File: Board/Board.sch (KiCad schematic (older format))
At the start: 14 parts

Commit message: Schematic and BOM almost done
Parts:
- removed MK?: Microphone, symbol Device:Microphone
- added C3, C7, C8: 100nF, Capacitor_SMD:C_0603_1608Metric, symbol Device:C
- added C6: 1000uF, symbol Device:C
- added D1: RED, LED_SMD:LED_0805_2012Metric, symbol Device:LED
- added MK1: IM69D120, Sensor_Audio:Infineon_PG-LLGA-5-1, symbol Sensor_Audio:IM69D120
- added Q1, Q2: Q_NMOS_GSD, Package_TO_SOT_SMD:SOT-23, symbol Device:Q_NMOS_GSD
- added R2, R5: 120, Resistor_SMD:R_0603_1608Metric, symbol Device:R
- added R3, R6: 510, Resistor_SMD:R_0603_1608Metric, symbol Device:R
- added R4: 3.48, Resistor_SMD:R_2512_6332Metric, symbol Device:R
- added SW2: SW_DIP_x01, symbol Switch:SW_DIP_x01
- added TP1, TP2, TP3, TP4, TP5, TP6: TestPoint, TestPoint:TestPoint_THTPad_D1.0mm_Drill0.5mm, symbol Connector:TestPoint
- BT1: renamed from BT?; footprint (none) -> Battery:BatteryHolder_Keystone_103_1x20mm
- C1, C4, C5: renamed from C?; footprint (none) -> Capacitor_SMD:C_0603_1608Metric
- C2: renamed from C?; value 22uF -> 33uF; footprint (none) -> Capacitor_SMD:C_0603_1608Metric
- J1: renamed from J?; footprint (none) -> Connector_Card:microSD_HC_Wuerth_693072010801
- L1: renamed from L?; footprint (none) -> Inductor_SMD:L_1206_3216Metric_Pad1.42x1.75mm_HandSolder
- LS1: renamed from LS?; footprint (none) -> Board:SPKR_CMS-151135-078S-67
- R1: renamed from R?; footprint (none) -> Resistor_SMD:R_0603_1608Metric
- gave numbers to parts that had none: 4
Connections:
- net labels added: +5V, CS, MCU_POWER, MICCLK, MICDATA, MISO, MOSI, RESET, SCK, SDPWR, SD_POWER, SPEAKER
- wire segments 18 -> 61
- no-connect marks 0 -> 15
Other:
- note added: "MICROCONTROLLER"
- note added: "MICROPHONE\n"
- note added: "POWER\n"
- note added: "SD CARD"
- note added: "SPEAKER\n"
- note added: "Should be 100\n"
- note added: "Should be 18pF"
- note added: "Should be 22uF"
- note removed: "TODO: Bien découpler\n"
- moved on the sheet: C1, C2, C4, C5, J1, L1, LS1, R1, U1, U2, Y1

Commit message: Schematic done, components almost selected
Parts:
- removed C3: 100nF, Capacitor_SMD:C_0603_1608Metric, symbol Device:C
- removed SW1: SW_Push, symbol Switch:SW_Push
- removed SW2: SW_DIP_x01, symbol Switch:SW_DIP_x01
- removed TP1, TP2, TP3, TP4, TP5, TP6: TestPoint, TestPoint:TestPoint_THTPad_D1.0mm_Drill0.5mm, symbol Connector:TestPoint
- added H1, H2, H3, H4, H5, H6, H7, H8: MountingHole_Pad, symbol Mechanical:MountingHole_Pad
- added R7: 10k, Resistor_SMD:R_0603_1608Metric, symbol Device:R
- added R?: 68, Resistor_SMD:R_0603_1608Metric, symbol Device:R
- added SW1, SW2: SW_SPST, symbol Switch:SW_SPST
- BT1: footprint Battery:BatteryHolder_Keystone_103_1x20mm -> (none)
- C2: value 33uF -> 22uF
- C4, C5: value 22pF -> 18pF
- R3, R6: value 510 -> 1k
- R5: value 120 -> 68
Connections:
- net labels added: SDGND
- net labels removed: SDPWR
- wire segments 61 -> 62
- no-connect marks 15 -> 14
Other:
- note removed: "Should be 100\n"
- note removed: "Should be 18pF"
- note removed: "Should be 22uF"
- moved on the sheet: C6, J1, LS1, Q1, Q2, R3, R4, R6

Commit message: BOM ready
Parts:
- removed BT1: Battery_Cell, symbol Device:Battery_Cell
- removed H1, H2, H3, H4, H5, H6, H7, H8: MountingHole_Pad, symbol Mechanical:MountingHole_Pad
- removed SW1: SW_SPST, symbol Switch:SW_SPST
- added J2: Conn_01x02_Male, ConnectorsEvo:B02B-PASK, symbol Connector:Conn_01x02_Male
- added TP1, TP2, TP3, TP4, TP5, TP6, TP7, TP8: TestPoint, TestPoint:TestPoint_THTPad_D1.0mm_Drill0.5mm, symbol Connector:TestPoint
- C2: footprint Capacitor_SMD:C_0603_1608Metric -> Capacitor_SMD:C_0805_2012Metric
- C6: footprint (none) -> Capacitor_THT:C_Radial_D8.0mm_H11.5mm_P3.50mm
- L1: footprint Inductor_SMD:L_1206_3216Metric_Pad1.42x1.75mm_HandSolder -> Inductor_SMD:L_1008_2520Metric
- SW2: footprint (none) -> Button_Switch_THT:SW_DIP_SPSTx01_Slide_6.7x4.1mm_W7.62mm_P2.54mm_LowProfile
- Y1: footprint (none) -> Crystal:Crystal_HC49-4H_Vertical
- gave numbers to parts that had none: 1
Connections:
- wire segments 62 -> 59

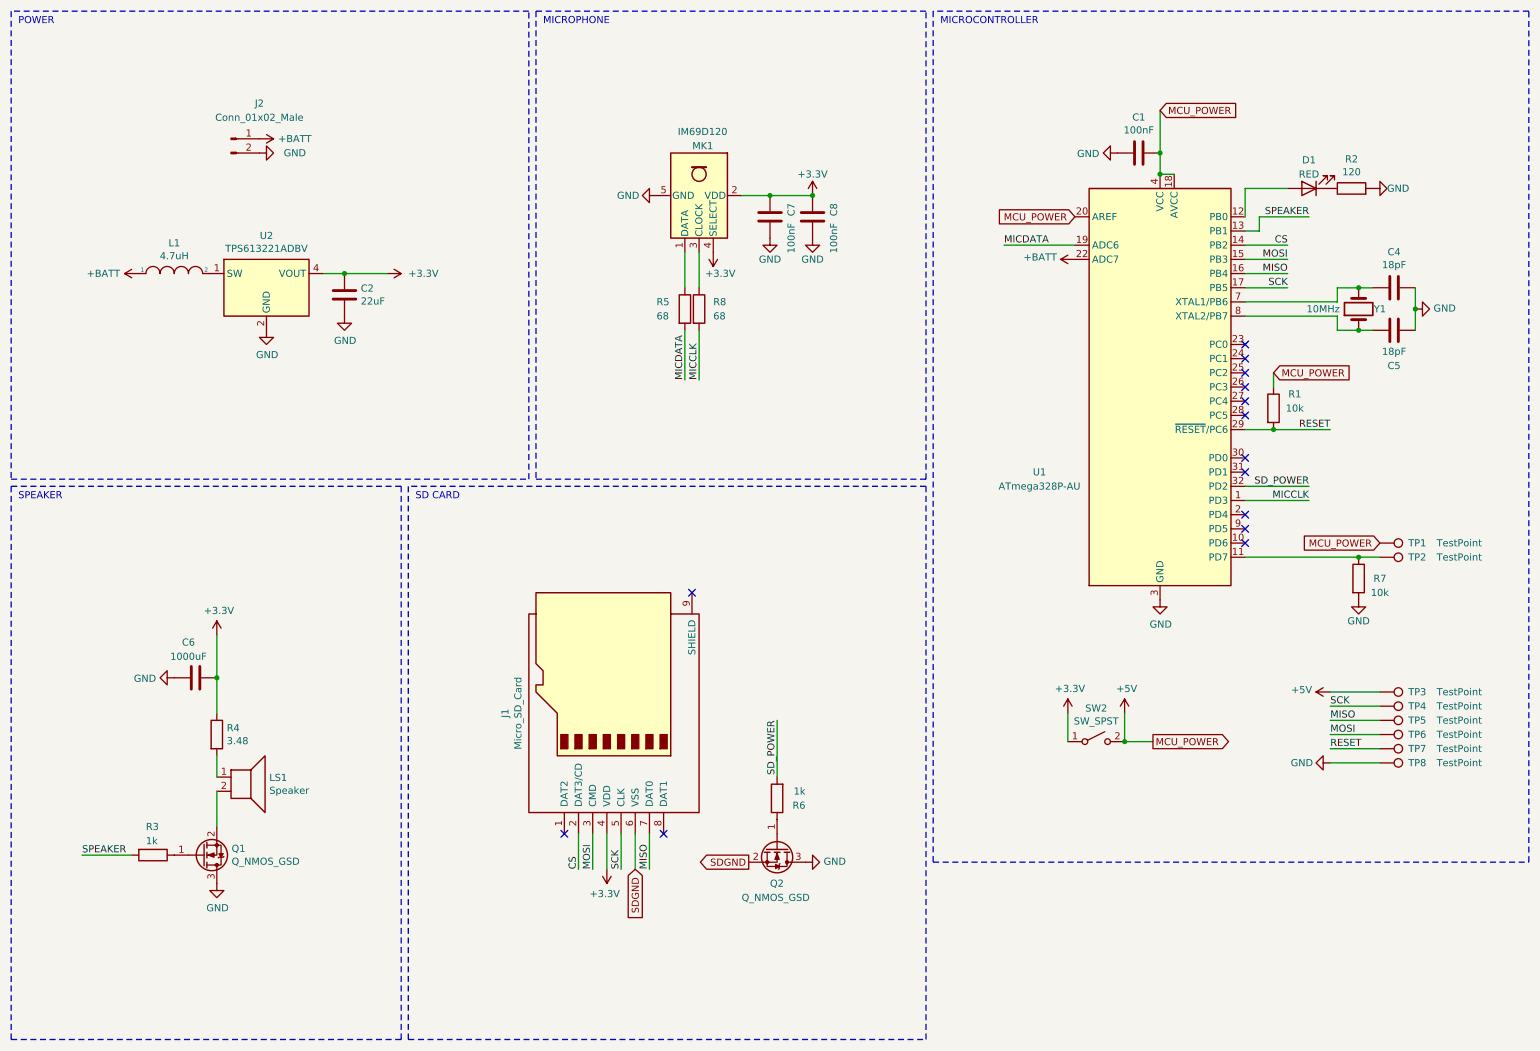
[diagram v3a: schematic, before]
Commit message: Changed components + first layout tests
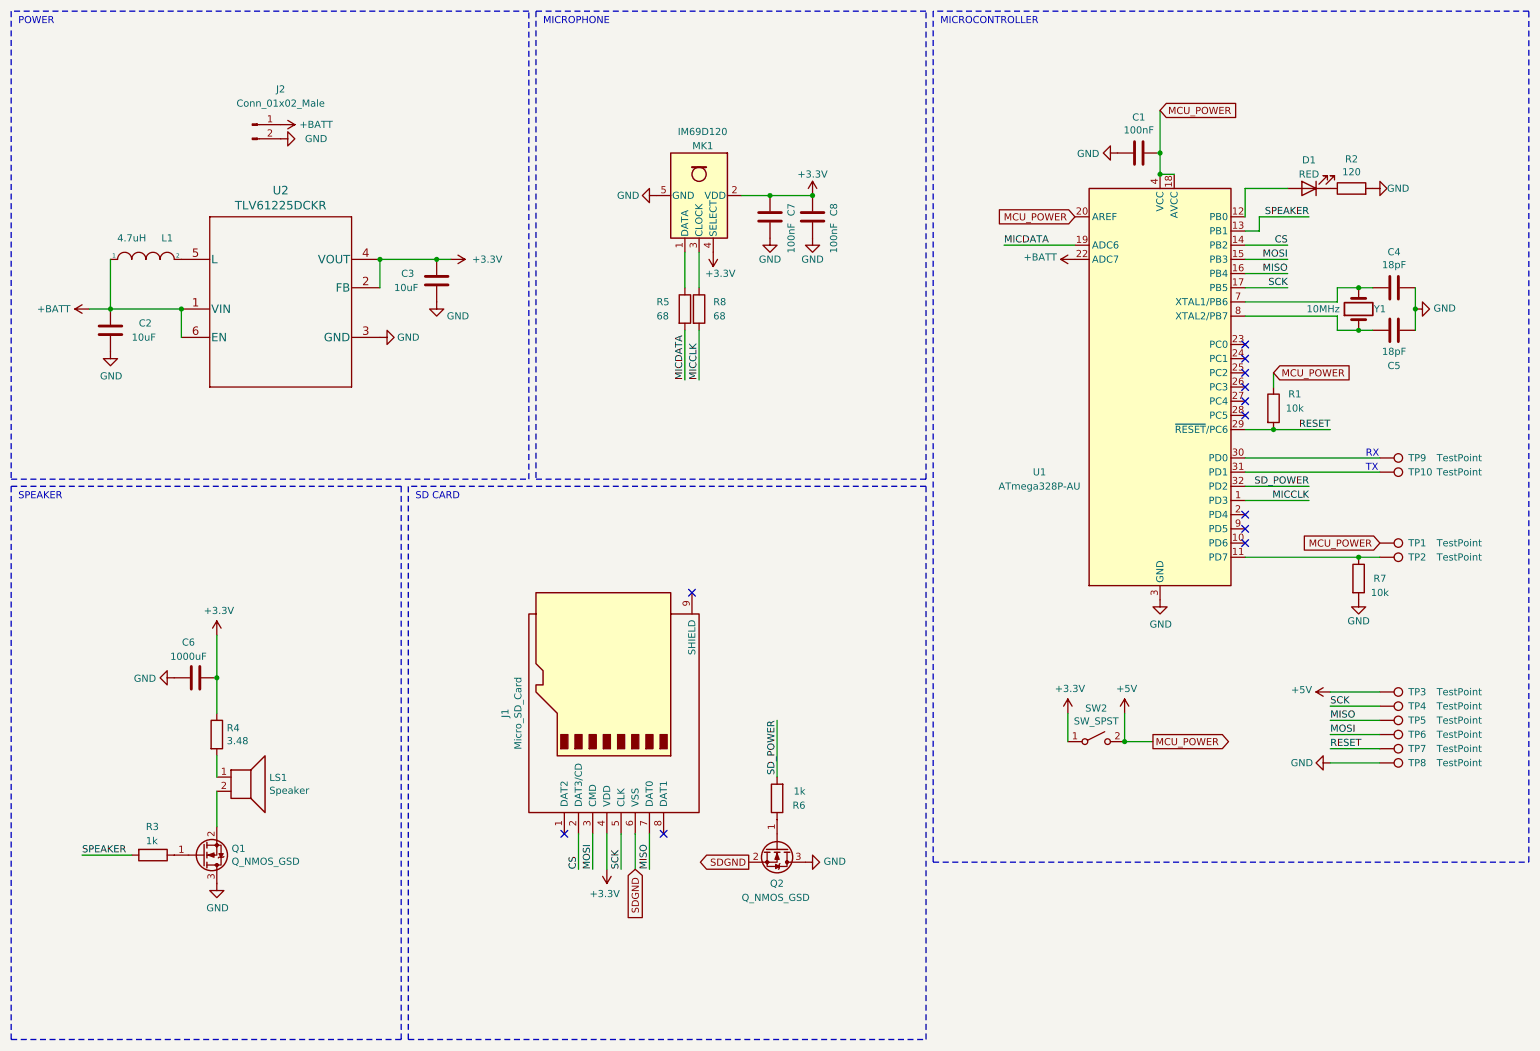
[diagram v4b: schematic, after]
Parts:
- removed U2: TPS613221ADBV, Package_TO_SOT_SMD:SOT-23-5, symbol Regulator_Switching:TPS613221ADBV
- added C3: 10uF, Capacitor_SMD:C_0805_2012Metric, symbol Device:C
- added TP10, TP9: TestPoint, TestPoint:TestPoint_THTPad_D1.0mm_Drill0.5mm, symbol Connector:TestPoint
- added U2: TLV61225DCKR, Board:SOT65P210X110-6N, symbol Symbols:TLV61225DCKR
- C2: value 22uF -> 10uF
- J2: footprint ConnectorsEvo:B02B-PASK -> ConnectorsEvo:S02B-PASK
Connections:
- net +3V3: now also C3.1, U2.2 (FB), U2.4 (VOUT); no longer C2.1
- net +BATT: now also C2.1, U2.1 (VIN), U2.6 (EN)
- net GND: now also C3.2, U2.3 (GND)
- net at U1.30 (PD0): now also TP9.1
- net at U1.31 (PD1): now also TP10.1
- net at L1.2: now also U2.5 (L)
- no-connect marks 14 -> 12
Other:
- note added: "RX"
- note added: "TX\n"
- moved on the sheet: J2
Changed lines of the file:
@@
 $EndDescr
-$Comp
-L MCU_Microchip_ATmega:ATmega328P-AU U1
-U 1 1 601056A9
-P 8600 3150
-F 0 "U1" H 7750 2550 50  0000 C CNN
-F 1 "ATmega328P-AU" H 7750 2450 50  0000 C CNN
-F 2 "Package_QFP:TQFP-32_7x7mm_P0.8mm" H 8600 3150 50  0001 C CIN
-F 3 "http://ww1.microchip.com/downloads/en/DeviceDoc/ATmega328_P%20AVR%20MCU%20with%20picoPower%20Technology%20Data%20Sheet%2040001984A.pdf" H 8600 3150 50  0001 C CNN
-	1    8600 3150
-	1    0    0    -1
-$EndComp
 $Comp
 L Connector:Micro_SD_Card J1
@@
 $EndComp
 $Comp
-L Regulator_Switching:TPS613221ADBV U2
-U 1 1 60105AB3
-P 2300 2450
-F 0 "U2" H 2300 2817 50  0000 C CNN
-F 1 "TPS613221ADBV" H 2300 2726 50  0000 C CNN
-F 2 "Package_TO_SOT_SMD:SOT-23-5" H 2300 1650 50  0001 C CNN
-F 3 "http://www.ti.com/lit/ds/symlink/tps61322.pdf" H 2300 2300 50  0001 C CNN
-	1    2300 2450
-	1    0    0    -1
-$EndComp
-$Comp
-L pspice:INDUCTOR L1
-U 1 1 60106C11
-P 1650 2350
-F 0 "L1" H 1650 2565 50  0000 C CNN
-F 1 "4.7uH" H 1650 2474 50  0000 C CNN
-F 2 "Inductor_SMD:L_1008_2520Metric" H 1650 2350 50  0001 C CNN
-F 3 "~" H 1650 2350 50  0001 C CNN
-	1    1650 2350
-	1    0    0    -1
-$EndComp
-$Comp
-L Device:C C2
-U 1 1 60107613
-P 2850 2500
-F 0 "C2" H 2965 2546 50  0000 L CNN
-F 1 "22uF" H 2965 2455 50  0000 L CNN
-F 2 "Capacitor_SMD:C_0805_2012Metric" H 2888 2350 50  0001 C CNN
-F 3 "~" H 2850 2500 50  0001 C CNN
-	1    2850 2500
-	1    0    0    -1
-$EndComp
-Wire Wire Line
-	2700 2350 2850 2350
-$Comp
-L power:GND #PWR0103
-U 1 1 601081F0
-P 2300 2750
-F 0 "#PWR0103" H 2300 2500 50  0001 C CNN
-F 1 "GND" H 2305 2577 50  0000 C CNN
-F 2 "" H 2300 2750 50  0001 C CNN
-F 3 "" H 2300 2750 50  0001 C CNN
-	1    2300 2750
-	1    0    0    -1
-$EndComp
-$Comp
-L power:+BATT #PWR0104
-U 1 1 6010A06B
-P 1400 2350
-F 0 "#PWR0104" H 1400 2200 50  0001 C CNN
-F 1 "+BATT" V 1400 2600 50  0000 C CNN
-F 2 "" H 1400 2350 50  0001 C CNN
-F 3 "" H 1400 2350 50  0001 C CNN
-	1    1400 2350
-	0    -1   -1   0
-$EndComp
-Wire Wire Line
-	2850 2350 3150 2350
-Connection ~ 2850 2350
-$Comp
-L power:+3.3V #PWR0105
-U 1 1 6010AFAD
-P 3150 2350
-F 0 "#PWR0105" H 3150 2200 50  0001 C CNN
-F 1 "+3.3V" V 3150 2500 50  0000 L CNN
-F 2 "" H 3150 2350 50  0001 C CNN
-F 3 "" H 3150 2350 50  0001 C CNN
-	1    3150 2350
-	0    1    1    0
-$EndComp
-$Comp
-L power:GND #PWR0106
-U 1 1 6010B535
-P 2850 2650
-F 0 "#PWR0106" H 2850 2400 50  0001 C CNN
-F 1 "GND" H 2855 2477 50  0000 C CNN
-F 2 "" H 2850 2650 50  0001 C CNN
-F 3 "" H 2850 2650 50  0001 C CNN
-	1    2850 2650
-	1    0    0    -1
-$EndComp
-$Comp
 L Device:C C1
 U 1 1 6010BA8F
@@
 Wire Wire Line
 	8600 1650 8700 1650
-Connection ~ 8600 1650
 $Comp
 L Device:R R1
@@
 	9400 3150 9400 3050
 NoConn ~ 9200 4050
-NoConn ~ 9200 3750
-NoConn ~ 9200 3650
 NoConn ~ 9200 3350
 NoConn ~ 9200 3250
@@
 L Connector:Conn_01x02_Male J2
 U 1 1 601DCBA6
-P 2050 1400
-F 0 "J2" H 2250 1650 50  0000 C CNN
-F 1 "Conn_01x02_Male" H 2250 1550 50  0000 C CNN
-F 2 "ConnectorsEvo:B02B-PASK" H 2050 1400 50  0001 C CNN
-F 3 "~" H 2050 1400 50  0001 C CNN
-	1    2050 1400
+P 2200 1300
+F 0 "J2" H 2400 1550 50  0000 C CNN
+F 1 "Conn_01x02_Male" H 2400 1450 50  0000 C CNN
+F 2 "ConnectorsEvo:S02B-PASK" H 2200 1300 50  0001 C CNN
+F 3 "~" H 2200 1300 50  0001 C CNN
+	1    2200 1300
 	1    0    0    -1
 $EndComp
@@
 L power:+BATT #PWR0101
 U 1 1 601DD392
-P 2250 1400
-F 0 "#PWR0101" H 2250 1250 50  0001 C CNN
-F 1 "+BATT" V 2250 1650 50  0000 C CNN
-F 2 "" H 2250 1400 50  0001 C CNN
-F 3 "" H 2250 1400 50  0001 C CNN
-	1    2250 1400
+P 2400 1300
+F 0 "#PWR0101" H 2400 1150 50  0001 C CNN
+F 1 "+BATT" V 2400 1550 50  0000 C CNN
+F 2 "" H 2400 1300 50  0001 C CNN
+F 3 "" H 2400 1300 50  0001 C CNN
+	1    2400 1300
 	0    1    1    0
 $EndComp
@@
 L power:GND #PWR0102
 U 1 1 601DE79F
-P 2250 1500
-F 0 "#PWR0102" H 2250 1250 50  0001 C CNN
-F 1 "GND" V 2250 1250 50  0000 C CNN
-F 2 "" H 2250 1500 50  0001 C CNN
-F 3 "" H 2250 1500 50  0001 C CNN
-	1    2250 1500
+P 2400 1400
+F 0 "#PWR0102" H 2400 1150 50  0001 C CNN
+F 1 "GND" V 2400 1150 50  0000 C CNN
+F 2 "" H 2400 1400 50  0001 C CNN
+F 3 "" H 2400 1400 50  0001 C CNN
+	1    2400 1400
 	0    -1   -1   0
 $EndComp
@@
 Wire Wire Line
 	9850 2650 9850 2750
+$Comp
+L power:GND #PWR012
+U 1 1 60205205
+P 3100 2800
+F 0 "#PWR012" H 3100 2550 50  0001 C CNN
+F 1 "GND" V 3100 2600 50  0000 C CNN
+F 2 "" H 3100 2800 50  0001 C CNN
+F 3 "" H 3100 2800 50  0001 C CNN
+	1    3100 2800
+	0    -1   -1   0
+$EndComp
+$Comp
+L power:+BATT #PWR010
+U 1 1 602057F1
+P 1050 2600
+F 0 "#PWR010" H 1050 2450 50  0001 C CNN
+F 1 "+BATT" V 1050 2850 50  0000 C CNN
+F 2 "" H 1050 2600 50  0001 C CNN
+F 3 "" H 1050 2600 50  0001 C CNN
+	1    1050 2600
+	0    -1   -1   0
+$EndComp
+$Comp
+L Device:C C2
+U 1 1 60208C6F
+P 1200 2750
+F 0 "C2" H 1400 2800 50  0000 L CNN
+F 1 "10uF" H 1350 2700 50  0000 L CNN
+F 2 "Capacitor_SMD:C_0805_2012Metric" H 1238 2600 50  0001 C CNN
+F 3 "~" H 1200 2750 50  0001 C CNN
+	1    1200 2750
+	1    0    0    -1
+$EndComp
+$Comp
+L power:GND #PWR011
+U 1 1 6020993C
+P 1200 2900
+F 0 "#PWR011" H 1200 2650 50  0001 C CNN
+F 1 "GND" H 1205 2727 50  0000 C CNN
+F 2 "" H 1200 2900 50  0001 C CNN
+F 3 "" H 1200 2900 50  0001 C CNN
+	1    1200 2900
+	1    0    0    -1
+$EndComp
+Wire Wire Line
+	1050 2600 1200 2600
+Connection ~ 1200 2600
+$Comp
+L pspice:INDUCTOR L1
+U 1 1 6020EEB9
+P 1450 2250
+F 0 "L1" H 1600 2400 50  0000 C CNN
+F 1 "4.7uH" H 1350 2400 50  0000 C CNN
+F 2 "Inductor_SMD:L_1008_2520Metric" H 1450 2250 50  0001 C CNN
+F 3 "~" H 1450 2250 50  0001 C CNN
+	1    1450 2250
+	1    0    0    -1
+$EndComp
+$Comp
+L Device:C C3
+U 1 1 60214C03
+P 3500 2400
+F 0 "C3" H 3250 2450 50  0000 L CNN
+F 1 "10uF" H 3200 2350 50  0000 L CNN
+F 2 "Capacitor_SMD:C_0805_2012Metric" H 3538 2250 50  0001 C CNN
+F 3 "~" H 3500 2400 50  0001 C CNN
+	1    3500 2400
+	1    0    0    -1
+$EndComp
+$Comp
+L power:GND #PWR013
+U 1 1 60214C09
+P 3500 2550
+F 0 "#PWR013" H 3500 2300 50  0001 C CNN
+F 1 "GND" H 3650 2450 50  0000 C CNN
+F 2 "" H 3500 2550 50  0001 C CNN
+F 3 "" H 3500 2550 50  0001 C CNN
+	1    3500 2550
+	1    0    0    -1
+$EndComp
+$Comp
+L power:+3.3V #PWR014
+U 1 1 60216211
+P 3600 2250
+F 0 "#PWR014" H 3600 2100 50  0001 C CNN
+F 1 "+3.3V" V 3600 2400 50  0000 L CNN
+F 2 "" H 3600 2250 50  0001 C CNN
+F 3 "" H 3600 2250 50  0001 C CNN
+	1    3600 2250
+	0    1    1    0
+$EndComp
+$Comp
+L Symbols:TLV61225DCKR U2
+U 1 1 60233EC8
+P 2400 2550
+F 0 "U2" H 2400 3336 60  0000 C CNN
+F 1 "TLV61225DCKR" H 2400 3230 60  0000 C CNN
+F 2 "Board:SOT65P210X110-6N" H 2400 1850 60  0001 C CNN
+F 3 "" H 2400 2550 60  0000 C CNN
+	1    2400 2550
+	1    0    0    -1
+$EndComp
+Wire Wire Line
+	1200 2600 1700 2600
+Wire Wire Line
+	1700 2600 1700 2800
+Connection ~ 1700 2600
+Wire Wire Line
+	1200 2600 1200 2250
+Wire Wire Line
+	3100 2450 3100 2250
+Wire Wire Line
+	3100 2250 3500 2250
+Connection ~ 3100 2250
+Connection ~ 3500 2250
+Wire Wire Line
+	3500 2250 3600 2250
+Connection ~ 8600 1650
+$Comp
+L MCU_Microchip_ATmega:ATmega328P-AU U1
+U 1 1 601056A9
+P 8600 3150
+F 0 "U1" H 7750 2550 50  0000 C CNN
+F 1 "ATmega328P-AU" H 7750 2450 50  0000 C CNN
+F 2 "Package_QFP:TQFP-32_7x7mm_P0.8mm" H 8600 3150 50  0001 C CIN
+F 3 "http://ww1.microchip.com/downloads/en/DeviceDoc/ATmega328_P%20AVR%20MCU%20with%20picoPower%20Technology%20Data%20Sheet%2040001984A.pdf" H 8600 3150 50  0001 C CNN
+	1    8600 3150
+	1    0    0    -1
+$EndComp
+$Comp
+L Connector:TestPoint TP9
+U 1 1 60201C0D
+P 10150 3650
+F 0 "TP9" V 10150 3850 50  0000 L CNN
+F 1 "TestPoint" V 10150 4050 50  0000 L CNN
+F 2 "TestPoint:TestPoint_THTPad_D1.0mm_Drill0.5mm" H 10350 3650 50  0001 C CNN
+F 3 "~" H 10350 3650 50  0001 C CNN
+	1    10150 3650
+	0    1    1    0
+$EndComp
+$Comp
+L Connector:TestPoint TP10
+U 1 1 60201C13
+P 10150 3750
+F 0 "TP10" V 10150 3950 50  0000 L CNN
+F 1 "TestPoint" V 10150 4150 50  0000 L CNN
+F 2 "TestPoint:TestPoint_THTPad_D1.0mm_Drill0.5mm" H 10350 3750 50  0001 C CNN
+F 3 "~" H 10350 3750 50  0001 C CNN
+	1    10150 3750
+	0    1    1    0
+$EndComp
+Wire Wire Line
+	9200 3650 10150 3650
+Wire Wire Line
+	9200 3750 10150 3750
+Text Notes 10050 3650 0    50   ~ 0
+RX
+Text Notes 10050 3750 0    50   ~ 0
+TX\n
 $EndSCHEMATC
